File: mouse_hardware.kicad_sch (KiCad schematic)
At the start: 48 parts, among them IC1 ADP150AUJZ-2.0-R7, IC2 AP2112K-3.3TRG1, J1 Conn_01x04_Pin, J2 Conn_01x04_Pin, SW1 SW_Push, SW5 SW_Push, U1 STM32F103RETx, U2 PMW3360DM-T2QU, Y1 8MHz

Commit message: Improve schematic
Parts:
- removed SW5: SW_Push, 147873-1:1478731, symbol Switch:SW_Push
- added C21: 100nF, Capacitor_SMD:C_0805_2012Metric_Pad1.18x1.45mm_HandSolder, symbol Device:C
- added SW2: SW_Push, 147873-1:1478731, symbol Switch:SW_Push
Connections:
- net DPI_SWITCH: now also U1.10 (PC2), SW2.1
- net GND: now also C21.2, SW2.2
- net LEFT_CLICK: now also U1.11 (PC3)
- net MIDDLE_CLICK: now also U1.25 (PC5)
- net MOTION: now also U1.9 (PC1); no longer U1.26 (PB0)
- net NRST: now also C21.1
- net RIGHT_CLICK: now also U1.24 (PC4)
- net STATUS_LED: now also U1.8 (PC0); no longer U1.14 (PA0)
- no-connect marks 39 -> 35

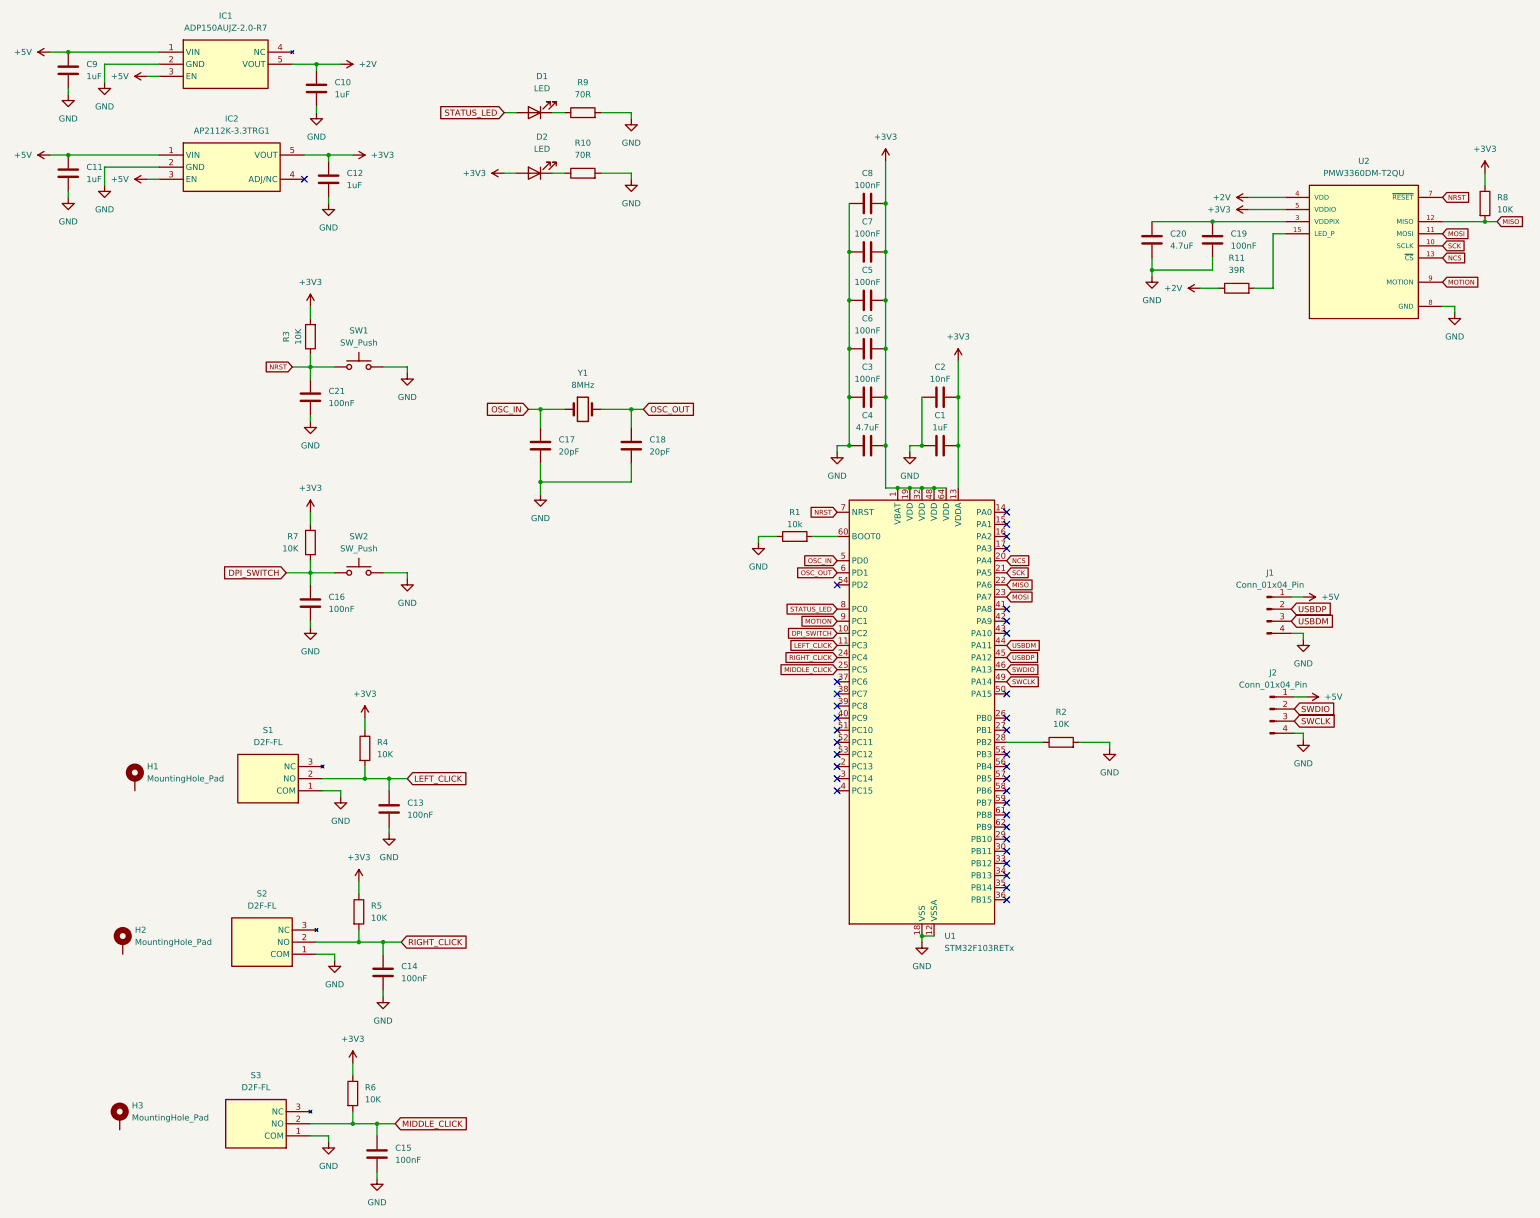
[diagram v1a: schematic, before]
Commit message: Re-reference and update pcb from schematic
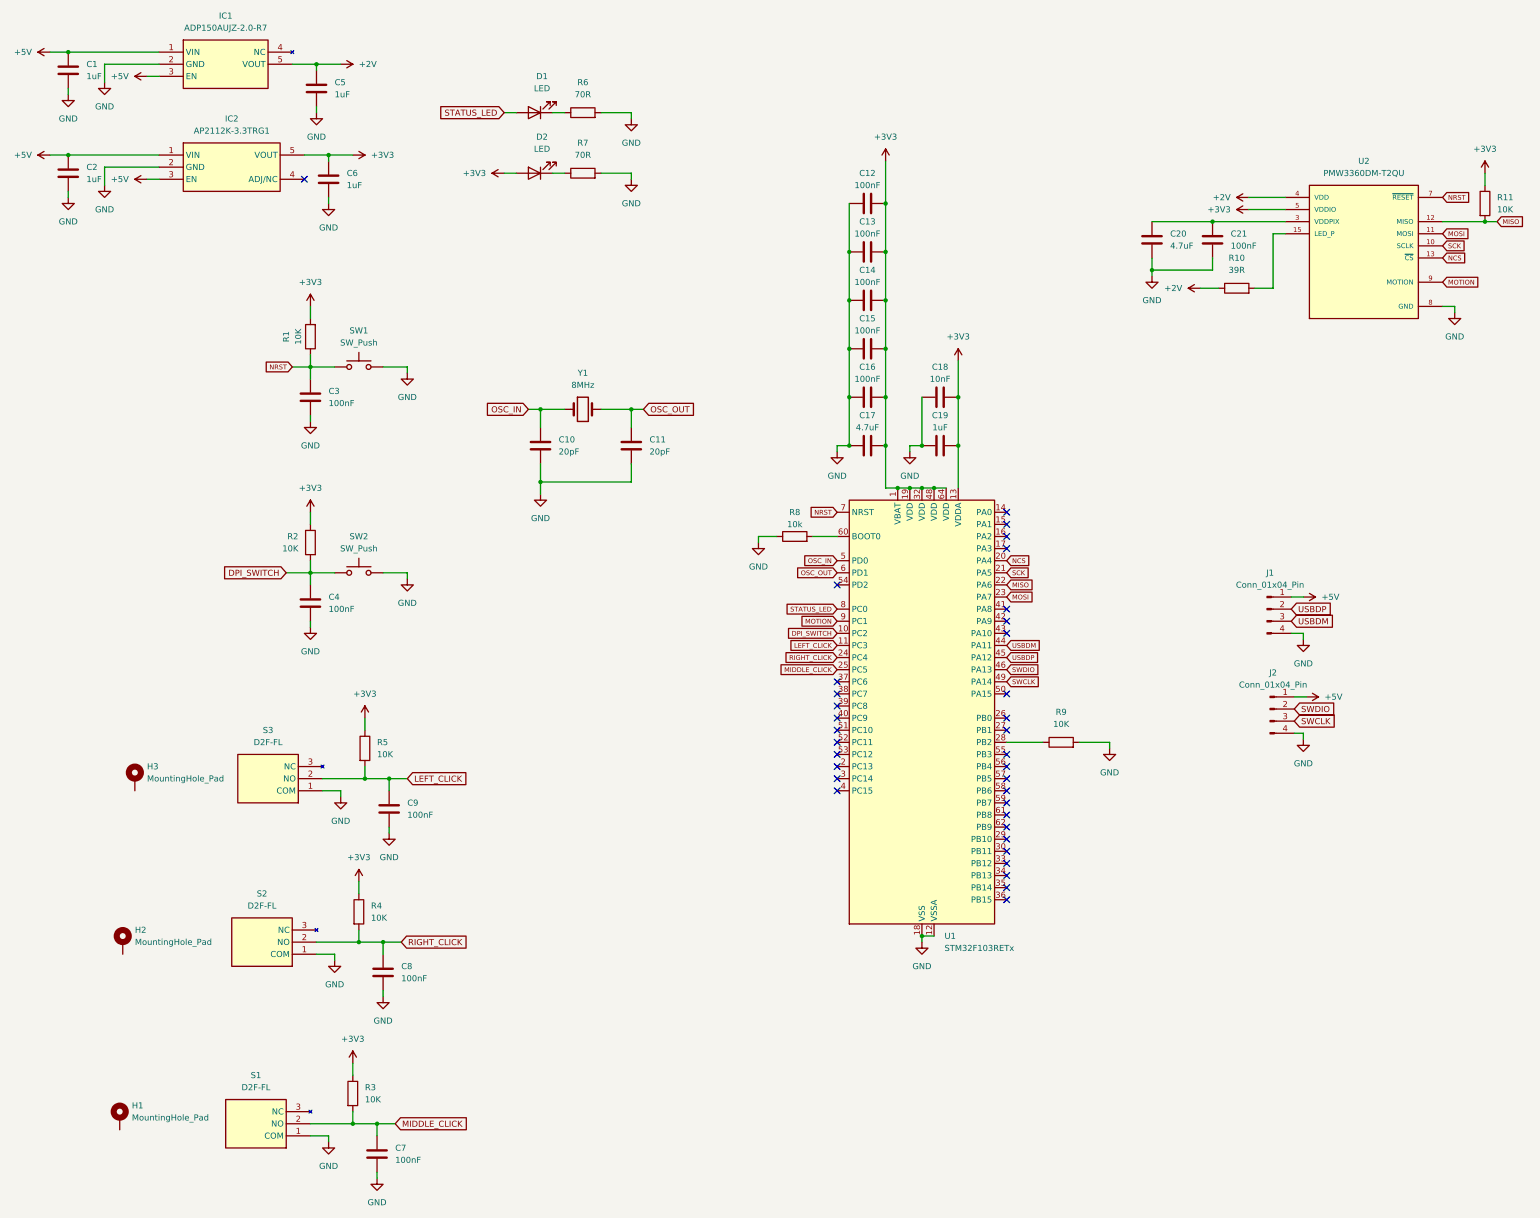
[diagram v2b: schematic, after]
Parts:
- renumbered C9 to C1, C17 to C10, C18 to C11, C8 to C12, C7 to C13, C5 to C14, C6 to C15, C3 to C16, C4 to C17, C2 to C18, C1 to C19, C11 to C2, C19 to C21, C21 to C3, C16 to C4, C10 to C5, C12 to C6, C15 to C7, C14 to C8, C13 to C9, H3 to H1, H1 to H3, R3 to R1, R11 to R10, R8 to R11, R7 to R2, R6 to R3, R5 to R4, R4 to R5, R9 to R6, R10 to R7, R1 to R8, R2 to R9, S3 to S1, S1 to S3

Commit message: Start re-routing
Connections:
- no-connect marks 35 -> 38
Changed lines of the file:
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@@
+	)
+	(no_connect
+		(at 41.275 254)
 	)
 	(no_connect
@@
 	)
 	(no_connect
+		(at 41.91 217.17)
+	)
+	(no_connect
 		(at 227.33 193.04)
 	)
@@
 	)
 	(no_connect
+		(at 44.45 182.88)
+	)
+	(no_connect
